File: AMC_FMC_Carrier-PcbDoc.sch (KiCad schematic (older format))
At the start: 16 parts

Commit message: pcb progress
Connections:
- wire segments 353 -> 332
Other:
- moved on the sheet: HS1
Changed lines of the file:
@@
 F9 "I2C_SFP2_SDA" B R 6800 13950 50
 F10 "I2C_SFP2_SCL" O R 6800 14050 50
-F11 "I2C_SFP3_SDA" B R 6800 14200 50
-F12 "I2C_SFP3_SCL" O R 6800 14300 50
-F13 "I2C_SFP4_SDA" B R 6800 14450 50
-F14 "I2C_SFP4_SCL" O R 6800 14550 50
 F15 "I2C_FMC1_SCL" O R 6800 13000 50
 F16 "I2C_FMC1_SDA" B R 6800 13100 50
@@
 	7550 7100 7550 6350
 Wire Wire Line
-	8200 13900 8550 13900
-Wire Wire Line
-	8000 14700 16350 14700
-Wire Wire Line
-	16350 14700 16350 12750
-Wire Wire Line
-	16350 12750 15650 12750
-Wire Wire Line
-	7950 14750 16300 14750
-Wire Wire Line
-	16300 14750 16300 12850
-Wire Wire Line
-	16300 12850 15650 12850
-Wire Wire Line
-	7800 14850 16050 14850
-Wire Wire Line
-	16050 14850 16050 13900
-Wire Wire Line
-	16050 13900 15650 13900
-Wire Wire Line
-	7750 14900 16000 14900
-Wire Wire Line
-	16000 14900 16000 14000
-Wire Wire Line
-	16000 14000 15650 14000
-Wire Wire Line
 	3900 12100 4150 12100
 Wire Wire Line
@@
 	6800 9950 11350 9950
 Wire Wire Line
-	6800 14550 7750 14550
-Wire Wire Line
-	7750 14550 7750 14900
-Wire Wire Line
-	6800 14450 7800 14450
-Wire Wire Line
-	7800 14450 7800 14850
-Wire Wire Line
-	6800 14300 7950 14300
-Wire Wire Line
-	7950 14300 7950 14750
-Wire Wire Line
-	6800 14200 8000 14200
-Wire Wire Line
-	8000 14200 8000 14700
-Wire Wire Line
-	6800 13950 8200 13950
-Wire Wire Line
-	8200 13950 8200 13900
-Wire Wire Line
 	6800 13800 8150 13800
 Wire Wire Line
@@
 Wire Wire Line
 	8000 12050 11350 12050
-Wire Wire Line
-	8250 14050 8250 14000
-Wire Wire Line
-	8250 14000 8550 14000
-Wire Wire Line
-	6800 14050 8250 14050
 Wire Wire Line
 	5100 13000 5000 13000
@@
 L Heat-Sinks:HSINK_ATS_ATS-50350B-C1-R0 HS1
 U 1 1 5D73CB17
-P 16600 2550
-F 0 "HS1" H 16600 2748 30  0000 C CNN
-F 1 "HS_AAVID_342947" H 16600 2475 50  0001 L CNN
-F 2 "po konwersji:HS_AAVID_342947" H 16600 2400 50  0001 L CNN
-F 3 "" H 16600 2325 50  0001 L CNN
-F 4 " " H 16600 2025 50  0001 L CNN "Comment"
-F 5 "HS_AAVID_342947" H 16600 2250 50  0001 L CNN "Part Number"
-F 6 "Heat Sink No Pad" H 16600 2175 50  0001 L CNN "Library Ref"
-F 7 "SchLib\\Heat-Sinks.SchLib" H 16600 2100 50  0001 L CNN "Library Path"
-F 8 "Standard" H 16600 1950 50  0001 L CNN "Component Kind"
-F 9 "Mechanical" H 16600 1875 50  0001 L CNN "Component Type"
-F 10 "0" H 16600 1800 50  0001 L CNN "Pin Count"
-F 11 " " H 16600 1725 50  0001 L CNN "Case"
-F 12 "PcbLib\\Heat-Sinks.PcbLib" H 16600 1650 50  0001 L CNN "Footprint Path"
-F 13 "HS_AAVID_342947" H 16600 1575 50  0001 L CNN "Footprint Ref"
-F 14 "35.0 x 35.0 x 7.5 mm BGA Heat Sink, Body 49.9mm x 35mm  Height 7.5mm" H 16600 1500 50  0001 L CNN "PackageDescription"
-F 15 "Yes" H 16600 1425 50  0001 L CNN "Mounted"
-F 16 "No" H 16600 1350 50  0001 L CNN "Socket"
-F 17 "No" H 16600 1275 50  0001 L CNN "SMD"
-F 18 "No" H 16600 1200 50  0001 L CNN "PressFit"
-F 19 "No" H 16600 1125 50  0001 L CNN "Sense"
-F 20 " " H 16600 1050 50  0001 L CNN "Sense Comment"
-F 21 "None" H 16600 975 50  0001 L CNN "Status"
-F 22 " " H 16600 900 50  0001 L CNN "Status Comment"
-F 23 " " H 16600 825 50  0001 L CNN "SCEM"
-F 24 "35.0 x 35.0 x 7.5 mm BGA Heat Sink - High Performance  maxiFLOW/maxiGRIP-STD" H 16600 750 50  0001 L CNN "Part Description"
-F 25 "ADVENCED THERMAL SOLUTION (ATS)" H 16600 675 50  0001 L CNN "Manufacturer"
-F 26 "HS_AAVID_342947" H 16600 600 50  0001 L CNN "Manufacturer Part Number"
-F 27 "7.5mm" H 16600 525 50  0001 L CNN "ComponentHeight"
-F 28 " " H 16600 450 50  0001 L CNN "Manufacturer1 Example"
-F 29 " " H 16600 375 50  0001 L CNN "Manufacturer1 Part Number"
-F 30 " " H 16600 300 50  0001 L CNN "Manufacturer1 ComponentHeight"
-F 31 " " H 16600 225 50  0001 L CNN "ComponentLink1Description"
-F 32 " " H 16600 150 50  0001 L CNN "ComponentLink2Description"
-F 33 "CERN DEM JLC" H 16600 75  50  0001 L CNN "Author"
-F 34 "11/30/16 00:00:00" H 16600 0   50  0001 L CNN "CreateDate"
-F 35 "11/30/16 00:00:00" H 16600 -75 50  0001 L CNN "LatestRevisionDate"
-F 36 "Heat-Sinks" H 16600 -150 50  0001 L CNN "Database Table Name"
-F 37 "Eletro-mechanical.DbLib" H 16600 -225 50  0001 L CNN "Library Name"
-F 38 "Heat-Sinks" H 16600 -300 50  0001 L CNN "Footprint Library"
-F 39 "This work is licensed under the Creative Commons CC-BY-SA 4.0 License. To the extent that circuit schematics that use Licensed Material can be considered to be ‘Adapted Material’, then the copyright holder waives article 3.b of the license with respect to these schematics." H 16600 -375 50  0001 L CNN "License"
-	1    16600 2550
+P 14650 2850
+F 0 "HS1" H 14650 3048 30  0000 C CNN
+F 1 "HS_AAVID_342947" H 14650 2775 50  0001 L CNN
+F 2 "po konwersji:HS_AAVID_342947" H 14650 2700 50  0001 L CNN
+F 3 "" H 14650 2625 50  0001 L CNN
+F 4 " " H 14650 2325 50  0001 L CNN "Comment"
+F 5 "HS_AAVID_342947" H 14650 2550 50  0001 L CNN "Part Number"
+F 6 "Heat Sink No Pad" H 14650 2475 50  0001 L CNN "Library Ref"
+F 7 "SchLib\\Heat-Sinks.SchLib" H 14650 2400 50  0001 L CNN "Library Path"
+F 8 "Standard" H 14650 2250 50  0001 L CNN "Component Kind"
+F 9 "Mechanical" H 14650 2175 50  0001 L CNN "Component Type"
+F 10 "0" H 14650 2100 50  0001 L CNN "Pin Count"
+F 11 " " H 14650 2025 50  0001 L CNN "Case"
+F 12 "PcbLib\\Heat-Sinks.PcbLib" H 14650 1950 50  0001 L CNN "Footprint Path"
+F 13 "HS_AAVID_342947" H 14650 1875 50  0001 L CNN "Footprint Ref"
+F 14 "35.0 x 35.0 x 7.5 mm BGA Heat Sink, Body 49.9mm x 35mm  Height 7.5mm" H 14650 1800 50  0001 L CNN "PackageDescription"
+F 15 "Yes" H 14650 1725 50  0001 L CNN "Mounted"
+F 16 "No" H 14650 1650 50  0001 L CNN "Socket"
+F 17 "No" H 14650 1575 50  0001 L CNN "SMD"
+F 18 "No" H 14650 1500 50  0001 L CNN "PressFit"
+F 19 "No" H 14650 1425 50  0001 L CNN "Sense"
+F 20 " " H 14650 1350 50  0001 L CNN "Sense Comment"
+F 21 "None" H 14650 1275 50  0001 L CNN "Status"
+F 22 " " H 14650 1200 50  0001 L CNN "Status Comment"
+F 23 " " H 14650 1125 50  0001 L CNN "SCEM"
+F 24 "35.0 x 35.0 x 7.5 mm BGA Heat Sink - High Performance  maxiFLOW/maxiGRIP-STD" H 14650 1050 50  0001 L CNN "Part Description"
+F 25 "ADVENCED THERMAL SOLUTION (ATS)" H 14650 975 50  0001 L CNN "Manufacturer"
+F 26 "HS_AAVID_342947" H 14650 900 50  0001 L CNN "Manufacturer Part Number"
+F 27 "7.5mm" H 14650 825 50  0001 L CNN "ComponentHeight"
+F 28 " " H 14650 750 50  0001 L CNN "Manufacturer1 Example"
+F 29 " " H 14650 675 50  0001 L CNN "Manufacturer1 Part Number"
+F 30 " " H 14650 600 50  0001 L CNN "Manufacturer1 ComponentHeight"
+F 31 " " H 14650 525 50  0001 L CNN "ComponentLink1Description"
+F 32 " " H 14650 450 50  0001 L CNN "ComponentLink2Description"
+F 33 "CERN DEM JLC" H 14650 375 50  0001 L CNN "Author"
+F 34 "11/30/16 00:00:00" H 14650 300 50  0001 L CNN "CreateDate"
+F 35 "11/30/16 00:00:00" H 14650 225 50  0001 L CNN "LatestRevisionDate"
+F 36 "Heat-Sinks" H 14650 150 50  0001 L CNN "Database Table Name"
+F 37 "Eletro-mechanical.DbLib" H 14650 75  50  0001 L CNN "Library Name"
+F 38 "Heat-Sinks" H 14650 0   50  0001 L CNN "Footprint Library"
+F 39 "This work is licensed under the Creative Commons CC-BY-SA 4.0 License. To the extent that circuit schematics that use Licensed Material can be considered to be ‘Adapted Material’, then the copyright holder waives article 3.b of the license with respect to these schematics." H 14650 -75 50  0001 L CNN "License"
+	1    14650 2850
 	1    0    0    -1
 $EndComp
@@
 F115 "MGT_TX_2_P" O R 12950 12750 50
 F116 "MGT_TX_2_N" O R 12950 12850 50
+F117 "QSFP_MOD_SEL" O R 12950 14050 50
+F118 "QSFP_RST" O R 12950 14150 50
+F119 "QSFP_MOD_PRS" O R 12950 14250 50
+F120 "QSFP_INT" I R 12950 14350 50
+F121 "QSFP_LPMODE" O R 12950 14450 50
 $EndSheet
 Wire Wire Line
@@
 Wire Wire Line
 	12950 13900 14150 13900
+Wire Wire Line
+	12950 14050 14150 14050
+Wire Wire Line
+	12950 14150 14150 14150
+Wire Wire Line
+	12950 14250 14150 14250
+Wire Wire Line
+	12950 14350 14150 14350
+Wire Wire Line
+	12950 14450 14150 14450
 $EndSCHEMATC

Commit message: FPGA power finished, significant progress on PCB
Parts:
- HS1: symbol Heat-Sinks:HSINK_ATS_ATS-50350B-C1-R0 -> AMC_FMC_Carrier-PcbDoc-rescue:HSINK_ATS_ATS-50350B-C1-R0-Heat-Sinks-AMC_FMC_Carrier-PcbDoc-rescue
- S1: symbol AMC_FMC_Carrier-PcbDoc-rescue:HDT0001-HDT0001 -> AMC_FMC_Carrier-PcbDoc-rescue:HDT0001-HDT0001-AMC_FMC_Carrier-PcbDoc-rescue-AMC_FMC_Carrier-PcbDoc-rescue
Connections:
- wire segments 332 -> 342
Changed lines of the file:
@@
 F7 "I2C_SFP1_SDA" B R 6800 13700 50
 F8 "I2C_SFP1_SCL" O R 6800 13800 50
-F9 "I2C_SFP2_SDA" B R 6800 13950 50
-F10 "I2C_SFP2_SCL" O R 6800 14050 50
-F15 "I2C_FMC1_SCL" O R 6800 13000 50
-F16 "I2C_FMC1_SDA" B R 6800 13100 50
-F17 "I2C_FMC2_SCL" O R 6800 13250 50
-F18 "I2C_FMC2_SDA" B R 6800 13350 50
-F19 "I2C_HDMI_SCL" O R 6800 13500 50
-F20 "I2C_HDMI_SDA" B R 6800 13600 50
+F9 "I2C_FMC1_SCL" O R 6800 13000 50
+F10 "I2C_FMC1_SDA" B R 6800 13100 50
+F11 "I2C_FMC2_SCL" O R 6800 13250 50
+F12 "I2C_FMC2_SDA" B R 6800 13350 50
+F13 "I2C_HDMI_SCL" O R 6800 13500 50
+F14 "I2C_HDMI_SDA" B R 6800 13600 50
+F15 "QSFP_SDA" B R 6800 14200 50
+F16 "QSFP_SCL" O R 6800 14300 50
 $EndSheet
 Wire Wire Line
@@
 FMC2_PRSNT_M2C_L
 $Comp
-L AMC_FMC_Carrier-PcbDoc-rescue:HDT0001-HDT0001 S1
+L AMC_FMC_Carrier-PcbDoc-rescue:HDT0001-HDT0001-AMC_FMC_Carrier-PcbDoc-rescue-AMC_FMC_Carrier-PcbDoc-rescue S1
 U 1 1 5DAB8DC7
 P 2950 9200
@@
 Wire Wire Line
 	1750 9300 1750 9450
-Wire Bus Line
-	7300 9450 6800 9450
 Text Label 6850 9450 0    50   ~ 10
 Pmod3_[0..7]
@@
 Marble v2
 $Comp
-L Heat-Sinks:HSINK_ATS_ATS-50350B-C1-R0 HS1
+L AMC_FMC_Carrier-PcbDoc-rescue:HSINK_ATS_ATS-50350B-C1-R0-Heat-Sinks-AMC_FMC_Carrier-PcbDoc-rescue HS1
 U 1 1 5D73CB17
 P 14650 2850
@@
 Wire Wire Line
 	12950 14450 14150 14450
+Wire Wire Line
+	6800 14200 10700 14200
+Wire Wire Line
+	10700 14200 10700 14850
+Wire Wire Line
+	10700 14850 15600 14850
+Wire Wire Line
+	15600 14850 15600 13350
+Wire Wire Line
+	15600 13350 15400 13350
+Wire Wire Line
+	6800 14300 10600 14300
+Wire Wire Line
+	10600 14300 10600 14950
+Wire Wire Line
+	10600 14950 15700 14950
+Wire Wire Line
+	15700 14950 15700 13450
+Wire Wire Line
+	15700 13450 15400 13450
+Wire Bus Line
+	6800 9450 7350 9450
 $EndSCHEMATC

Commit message: new board outline, rearranging banks connections, SODIMM memory
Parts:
- removed HS1: HS_AAVID_342947, po konwersji:HS_AAVID_342947, symbol AMC_FMC_Carrier-PcbDoc-rescue:HSINK_ATS_ATS-50350B-C1-R0-Heat-Sinks-AMC_FMC_Car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
- S1: symbol AMC_FMC_Carrier-PcbDoc-rescue:HDT0001-HDT0001-AMC_FMC_Carrier-PcbDoc-rescue-AMC_FMC_Carrier-PcbDoc-rescue -> AMC_FMC_Carrier-PcbDoc-rescue:HDT0001-HDT0001-AMC_FMC_Carrier-PcbDoc-rescue
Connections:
- net labels added: MUX1_MMC, MUX2_MMC, MUX3_MMC
- wire segments 342 -> 357
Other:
- note added: "CLK CONF"
- note added: "QSFP 1"
- note added: "QSFP 2"
- note removed: "CLK"
- note removed: "SFP1"

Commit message: DDR fanout done
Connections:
- net labels added: I2C_PM_SCL, I2C_PM_SDA
- wire segments 357 -> 359
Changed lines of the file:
@@
 Wire Wire Line
 	12950 4700 14150 4700
+Wire Wire Line
+	15650 3250 16300 3250
+Text Label 15800 3250 0    50   ~ 10
+I2C_PM_SDA
+Text Label 15800 3350 0    50   ~ 10
+I2C_PM_SCL
+Wire Wire Line
+	16300 3350 15650 3350
 $EndSCHEMATC

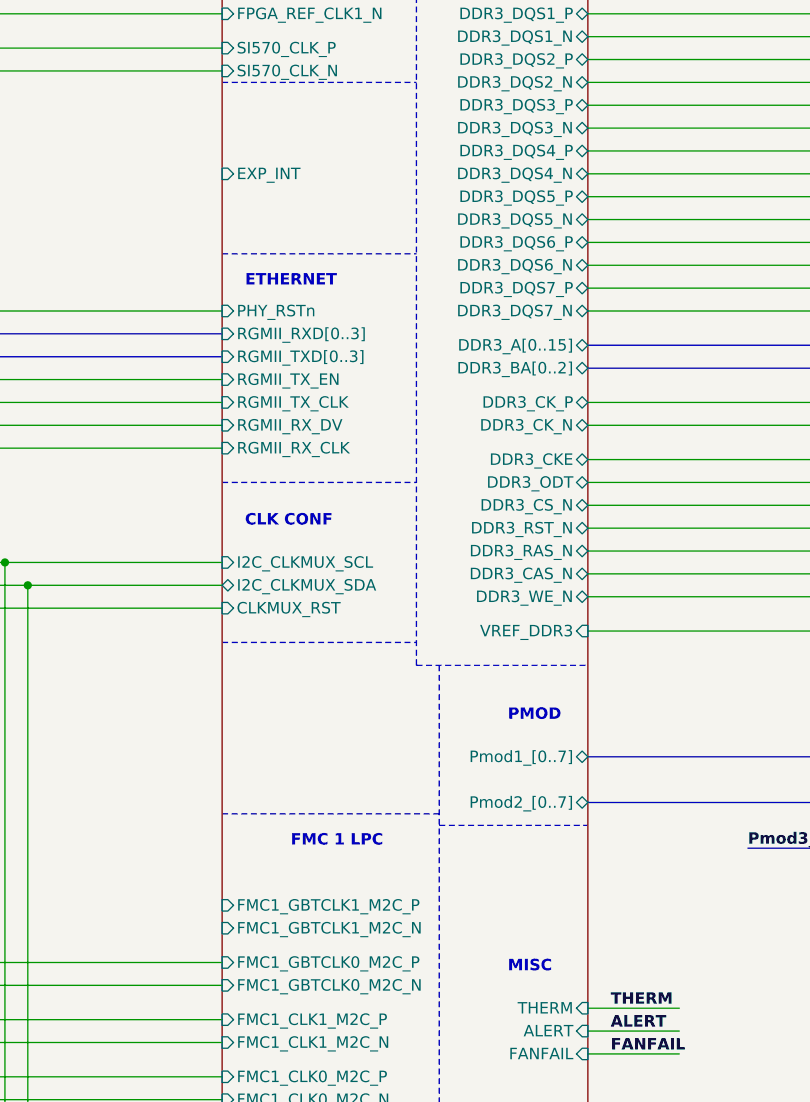
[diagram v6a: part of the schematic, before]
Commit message: FMC1 fanout and routing
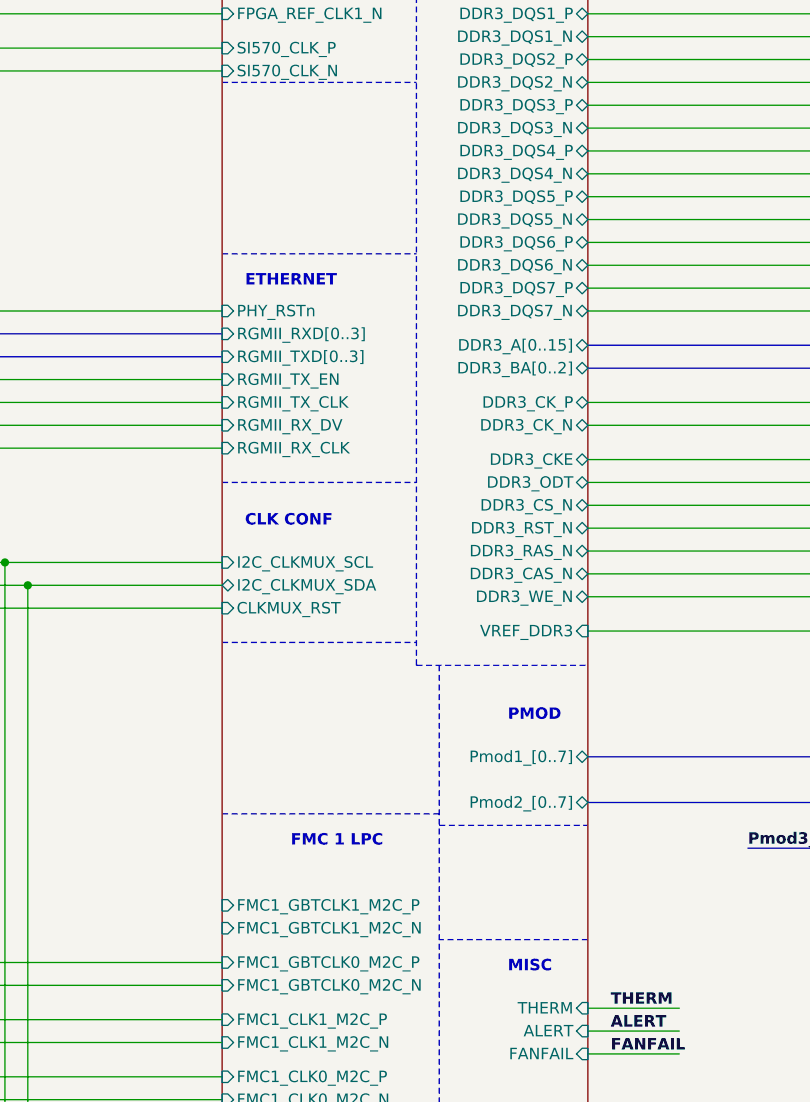
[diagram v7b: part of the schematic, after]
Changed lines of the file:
@@
 F140 "DDR3_CAS_N" B R 12950 5350 50
 F141 "DDR3_WE_N" B R 12950 5450 50
-F142 "EXP_INT" I L 11350 3600 50
-F143 "DDR3_CS_N" B R 12950 5050 50
-F144 "DDR3_DQS0_P" B R 12950 2700 50
-F145 "DDR3_DQS0_N" B R 12950 2800 50
-F146 "DDR3_DQS1_P" B R 12950 2900 50
-F147 "DDR3_DQS1_N" B R 12950 3000 50
-F148 "DDR3_DQS2_P" B R 12950 3100 50
-F149 "DDR3_DQS2_N" B R 12950 3200 50
-F150 "DDR3_DQS3_P" B R 12950 3300 50
-F151 "DDR3_DQS3_N" B R 12950 3400 50
-F152 "DDR3_DM[0..3]" B R 12950 2450 50
-F153 "DDR3_DQ[0..31]" B R 12950 2200 50
-F154 "VREF_DDR3" I R 12950 5600 50
+F142 "DDR3_CS_N" B R 12950 5050 50
+F143 "DDR3_DQS0_P" B R 12950 2700 50
+F144 "DDR3_DQS0_N" B R 12950 2800 50
+F145 "DDR3_DQS1_P" B R 12950 2900 50
+F146 "DDR3_DQS1_N" B R 12950 3000 50
+F147 "DDR3_DQS2_P" B R 12950 3100 50
+F148 "DDR3_DQS2_N" B R 12950 3200 50
+F149 "DDR3_DQS3_P" B R 12950 3300 50
+F150 "DDR3_DQS3_N" B R 12950 3400 50
+F151 "DDR3_DM[0..3]" B R 12950 2450 50
+F152 "DDR3_DQ[0..31]" B R 12950 2200 50
+F153 "VREF_DDR3" I R 12950 5600 50
 $EndSheet
 Wire Notes Line
@@
 Wire Wire Line
 	16300 3350 15650 3350
+Wire Notes Line
+	12950 6950 12300 6950
 $EndSCHEMATC

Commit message: routing progress
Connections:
- wire segments 359 -> 363
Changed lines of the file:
@@
 $EndDescr
-$Sheet
-S 8500 7950 1550 1550
-U 5BD31F9F
-F0 "FMC_2" 50
-F1 "FMC_2.sch" 50
-F2 "FMC2_GBTCLK0_M2C_P" O R 10050 8850 50
-F3 "FMC2_GBTCLK0_M2C_N" O R 10050 8950 50
-F4 "FMC2_CLK1_M2C_P" O R 10050 9100 50
-F5 "FMC2_CLK1_M2C_N" O R 10050 9200 50
-F6 "FMC2_CLK0_M2C_P" O R 10050 9350 50
-F7 "FMC2_CLK0_M2C_N" O R 10050 9450 50
-F8 "FMC2_PRSNT_M2C_L" O L 8500 8250 50
-F9 "I2C_FMC2_SCL" I L 8500 8350 50
-F10 "I2C_FMC2_SDA" B L 8500 8450 50
-F11 "FMC2_TCK" I L 8500 8600 50
-F12 "FMC2_TDI" I L 8500 8700 50
-F13 "FMC2_TDO" O L 8500 8800 50
-F14 "FMC2_TMS" I L 8500 8900 50
-F15 "FMC2_TRST" I L 8500 9000 50
-F16 "FMC2_PG_C2M" O L 8500 8150 50
-F17 "FMC2_FUSE" O L 8500 9100 50
-$EndSheet
 $Sheet
 S 14150 2000 1500 3700
@@
 F16 "FMC1_PG_C2M" O L 8500 6350 50
 F17 "FMC1_FUSE" O L 8500 7300 50
+F18 "FMC1_GBTCLK1_M2C_P" O R 10050 6800 50
+F19 "FMC1_GBTCLK1_M2C_N" O R 10050 6900 50
 $EndSheet
 $Comp
@@
 Wire Notes Line
 	12950 6950 12300 6950
+$Sheet
+S 8500 7950 1550 1550
+U 5BD31F9F
+F0 "FMC_2" 50
+F1 "FMC_2.sch" 50
+F2 "FMC2_GBTCLK0_M2C_P" O R 10050 8850 50
+F3 "FMC2_GBTCLK0_M2C_N" O R 10050 8950 50
+F4 "FMC2_CLK1_M2C_P" O R 10050 9100 50
+F5 "FMC2_CLK1_M2C_N" O R 10050 9200 50
+F6 "FMC2_CLK0_M2C_P" O R 10050 9350 50
+F7 "FMC2_CLK0_M2C_N" O R 10050 9450 50
+F8 "FMC2_PRSNT_M2C_L" O L 8500 8250 50
+F9 "I2C_FMC2_SCL" I L 8500 8350 50
+F10 "I2C_FMC2_SDA" B L 8500 8450 50
+F11 "FMC2_TCK" I L 8500 8600 50
+F12 "FMC2_TDI" I L 8500 8700 50
+F13 "FMC2_TDO" O L 8500 8800 50
+F14 "FMC2_TMS" I L 8500 8900 50
+F15 "FMC2_TRST" I L 8500 9000 50
+F16 "FMC2_PG_C2M" O L 8500 8150 50
+F17 "FMC2_FUSE" O L 8500 9100 50
+F18 "FMC2_GBTCLK1_M2C_P" O R 10050 8600 50
+F19 "FMC2_GBTCLK1_M2C_N" O R 10050 8700 50
+$EndSheet
+Wire Wire Line
+	10050 8600 11350 8600
+Wire Wire Line
+	10050 8700 11350 8700
+Wire Wire Line
+	10050 6900 11350 6900
+Wire Wire Line
+	10050 6800 11350 6800
 $EndSCHEMATC
